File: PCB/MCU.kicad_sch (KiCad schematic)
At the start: 54 parts, among them J301 Conn_01x03_Pin, J302 Conn_01x10_Pin, J303 STLink Connector, Q301 S9013, SW301 PTS647SM70SMTR2LFS, SW302 PTS647SM70SMTR2LFS, SW303 SW_DPDT_x2, U301 STM32F411RET6, U302 STM32F103CBT6, U303 LTST-C155KGJRKT, U304 MAX7375AXR805, U305 MAX7375AXR805

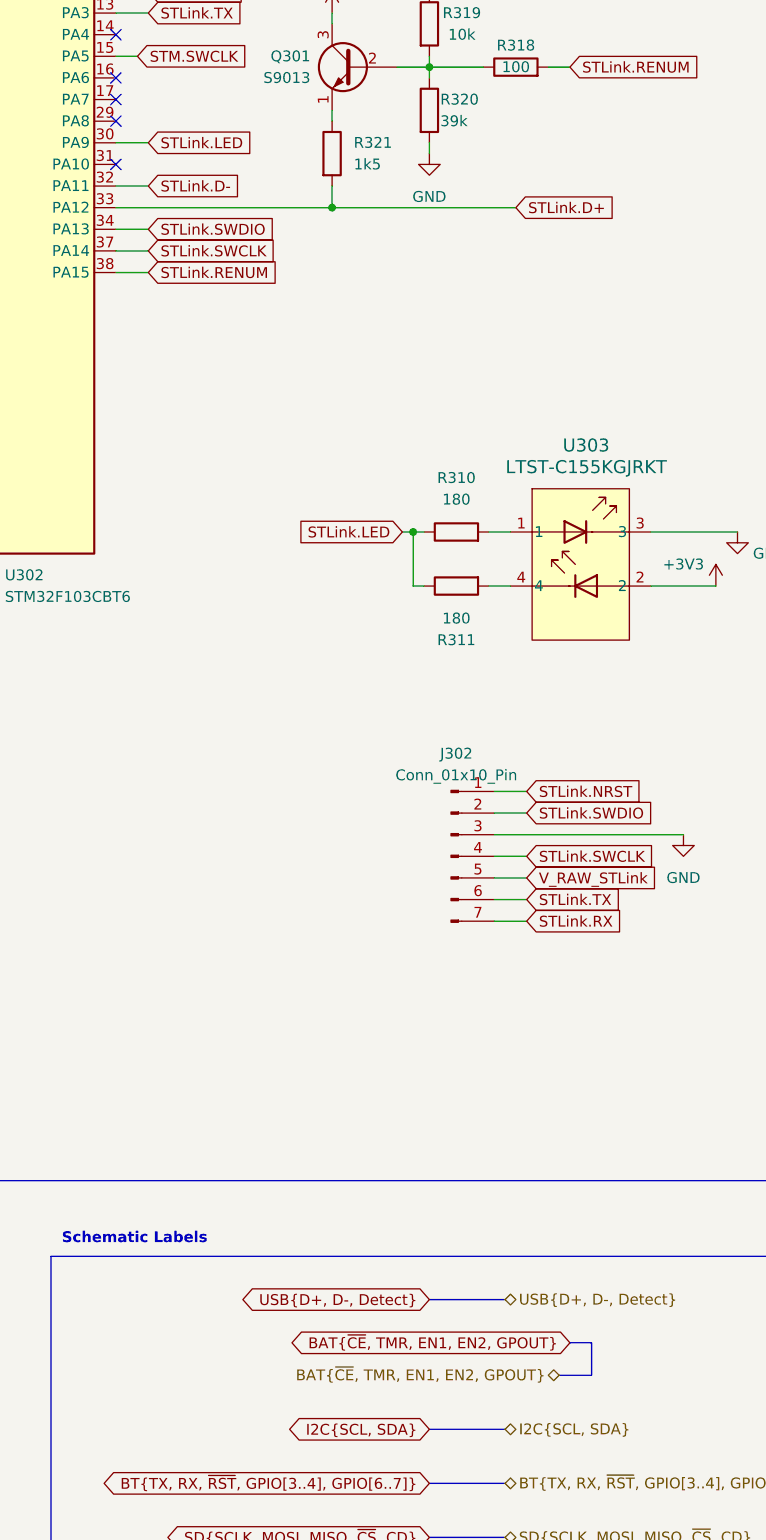
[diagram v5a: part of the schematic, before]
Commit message: Redesign bluetooth of v2
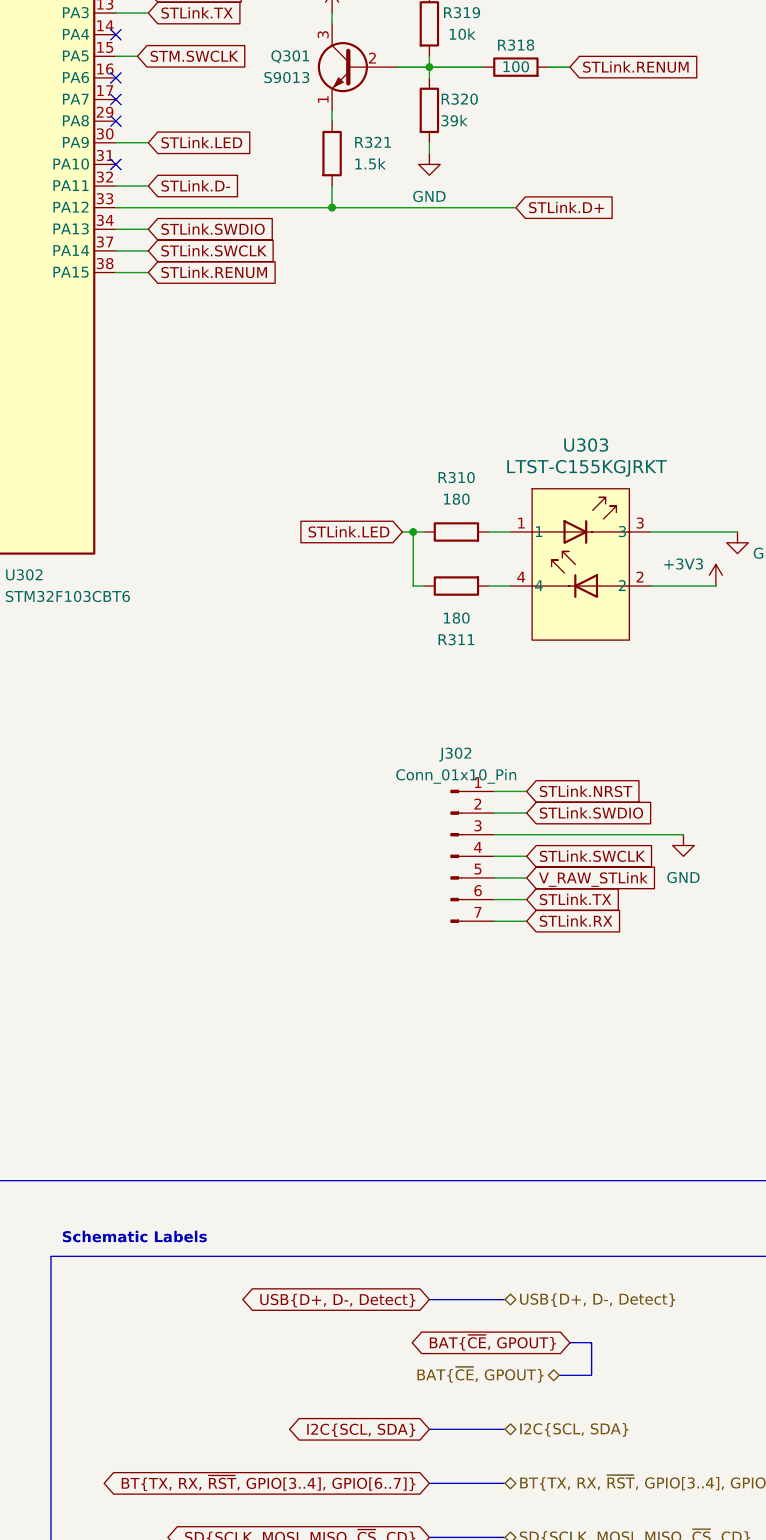
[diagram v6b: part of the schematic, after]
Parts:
- C301, C302, C303, C304, C305, C306, C307, C308, C309, C310, C313, C314, C315, C316, C317, C318, C319, C320, FB301, R301, R304, R305, R306, R307, R308, R309, R310, R311, R312, R313, R314, R315, R316, R317, R318, R319, R320: Package 0603 -> (none)
- D301: Package SOD-523 -> (none)
- D302: Package SOD-128 -> (none)
- D303, D304: footprint Diode_SMD:D_0805_2012Metric_Pad1.15x1.40mm_HandSolder -> LED_SMD:LED_0805_2012Metric_Pad1.15x1.40mm_HandSolder; Manufacturer ams-OSRAM USA INC. -> Würth Elektronik; Mfg. Part # LS R976-NR-1 -> 150080BS75000; Package 0805 -> (none); Supplier Part # 475-LSR976-NR-1CT-ND -> 732-4982-1-ND
- J301, J302: Supplier Amazon -> N/A
- J303: Package CONN10_302-S101_OST -> (none)
- Q301: Package SOT-23-3 -> (none)
- R321: value 1k5 -> 1.5k; Package 0603 -> (none)
- SW301, SW302: Package PTS647SM70SMTR2LFS_CNK -> (none)
- SW303: Package JS202011SCQN -> (none)
- U301: Package 64-LQFP -> (none)
- U302: Package 48-LQFP -> (none)
- U303: Package 1210 -> (none)
- U304, U305: Package SOT-323 -> (none)

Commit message: Update PCB Design v2
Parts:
- added J304, J305: Conn_01x03_Pin, Connector_PinHeader_2.54mm:PinHeader_1x03_P2.54mm_Vertical, symbol Connector:Conn_01x03_Pin
- C301, C302, C303, C304, C305, C306, C307, C308, C309, C313, C314, C315, C316, C317, C318, C319, C320: footprint Capacitor_SMD:C_0603_1608Metric_Pad1.08x0.95mm_HandSolder -> Capacitor_SMD:C_0805_2012Metric_Pad1.18x1.45mm_HandSolder; Manufacturer Murata Electronics -> Samsung Electro-Mechanics; Mfg. Part # GRM033R61A104ME15D -> CL21B104KBCNNNC; Supplier Part # 490-5405-1-ND -> 1276-1003-1-ND
- C310: footprint Capacitor_SMD:C_0603_1608Metric_Pad1.08x0.95mm_HandSolder -> Capacitor_SMD:C_0805_2012Metric_Pad1.18x1.45mm_HandSolder; Manufacturer Murata Electronics -> Samsung Electro-Mechanics; Mfg. Part # GRM188R61E225KA12D -> CL21B225KAFNFNE; Supplier Part # 490-10731-1-ND -> 1276-2953-1-ND
- J301: now left out of the parts list
- R301, R304, R305, R309: footprint Resistor_SMD:R_0603_1608Metric_Pad0.98x0.95mm_HandSolder -> Resistor_SMD:R_0805_2012Metric_Pad1.20x1.40mm_HandSolder; Mfg. Part # RC0603FR-07100KL -> RC0805FR-07100KL; Supplier Part # 311-100KHRCT-ND -> 311-100KCRCT-ND
- R306, R312, R313: footprint Resistor_SMD:R_0603_1608Metric_Pad0.98x0.95mm_HandSolder -> Resistor_SMD:R_0805_2012Metric_Pad1.20x1.40mm_HandSolder; Mfg. Part # RC0603FR-074K7L -> RC0805JR-074K7L; Supplier Part # 311-4.70KHRCT-ND -> 311-4.7KARCT-ND
- R307: footprint Resistor_SMD:R_0603_1608Metric_Pad0.98x0.95mm_HandSolder -> Resistor_SMD:R_0805_2012Metric_Pad1.20x1.40mm_HandSolder; Manufacturer RMCF0603FT2K70 -> YAGEO; Mfg. Part # RMCF0603FT2K70 -> RC0805JR-072K7L; Supplier Part # RMCF0603FT2K70CT-ND -> 311-2.7KARCT-ND
- R308, R317, R319: footprint Resistor_SMD:R_0603_1608Metric_Pad0.98x0.95mm_HandSolder -> Resistor_SMD:R_0805_2012Metric_Pad1.20x1.40mm_HandSolder; Mfg. Part # RC0603JR-0710KL -> RC0805FR-0710KL; Supplier Part # 311-10KGRCT-ND -> 311-10.0KCRCT-ND
- R310, R311: footprint Resistor_SMD:R_0603_1608Metric_Pad0.98x0.95mm_HandSolder -> Resistor_SMD:R_0805_2012Metric_Pad1.20x1.40mm_HandSolder; Mfg. Part # RC0603FR-13180RL -> RC0805JR-07180RL; Supplier Part # 13-RC0603FR-13180RLCT-ND -> 311-180ARCT-ND
- R314, R315: value 250 -> 330; footprint Resistor_SMD:R_0603_1608Metric_Pad0.98x0.95mm_HandSolder -> Resistor_SMD:R_0805_2012Metric_Pad1.20x1.40mm_HandSolder; Manufacturer Stackpole Electronics Inc -> YAGEO; Mfg. Part # RNCF0603TKY250R -> RC0805FR-07330RL; Supplier Part # RNCF0603TKY250RCT-ND -> 311-330CRCT-ND
- R316, R318: footprint Resistor_SMD:R_0603_1608Metric_Pad0.98x0.95mm_HandSolder -> Resistor_SMD:R_0805_2012Metric_Pad1.20x1.40mm_HandSolder; Mfg. Part # RC0603FR-07100RL -> RC0805FR-07100RL; Supplier Part # 311-100HRCT-ND -> 311-100CRCT-ND
- R320: footprint Resistor_SMD:R_0603_1608Metric_Pad0.98x0.95mm_HandSolder -> Resistor_SMD:R_0805_2012Metric_Pad1.20x1.40mm_HandSolder; Mfg. Part # RC0603JR-0739KL -> RC0805FR-0739KL; Supplier Part # 311-39KGRCT-ND -> 311-39.0KCRCT-ND
- R321: footprint Resistor_SMD:R_0603_1608Metric_Pad0.98x0.95mm_HandSolder -> Resistor_SMD:R_0805_2012Metric_Pad1.20x1.40mm_HandSolder; Mfg. Part # RC0603FR-131K5L -> RC0805FR-071K5L; Supplier Part # 13-RC0603FR-131K5LCT-ND -> 311-1.50KCRCT-ND
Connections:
- net GND: now also J304.1 (Pin_1), J304.2 (Pin_2), J304.3 (Pin_3), J305.1 (Pin_1), J305.2 (Pin_2), J305.3 (Pin_3)
